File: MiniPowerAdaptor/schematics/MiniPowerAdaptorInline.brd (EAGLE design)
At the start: 20.3 x 19.1 mm, 8 parts, among them IC1 LM317MBSTT3

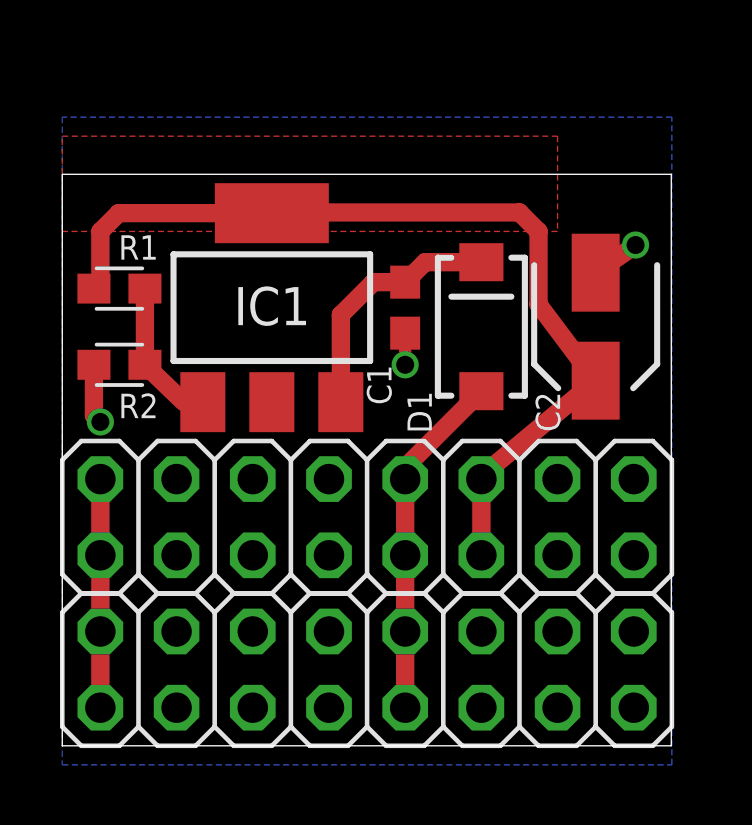
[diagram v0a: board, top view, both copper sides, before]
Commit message: inline 5v adaptor ordered from seeed
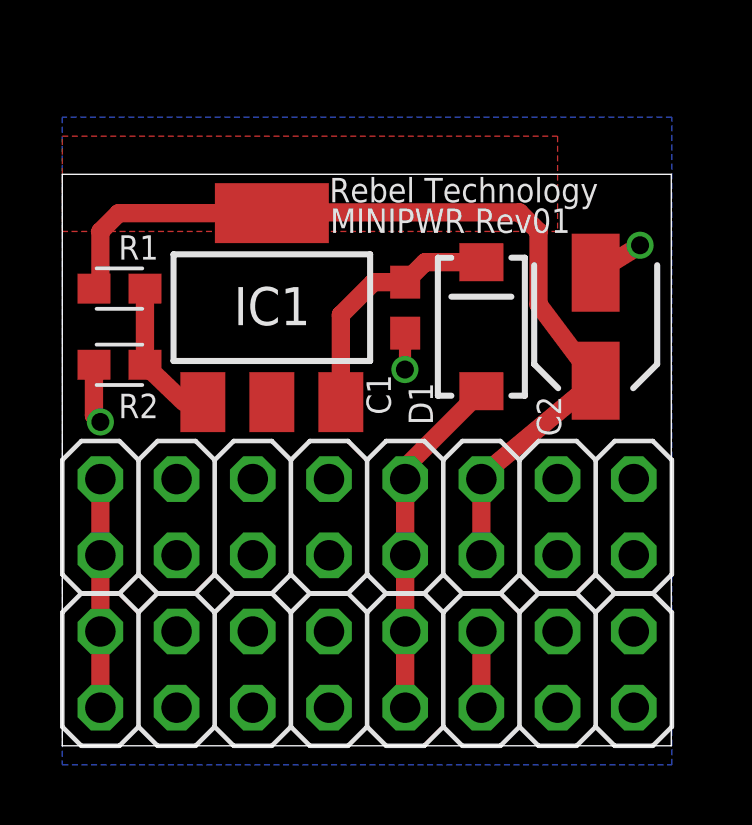
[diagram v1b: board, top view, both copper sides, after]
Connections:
- new net N$2: IN.11, IN.12
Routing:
- net N$2: track 0.00 -> 2.54 mm
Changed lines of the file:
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@@
 <setting verticaltext="up"/>
 </settings>
-<grid distance="0.05" unitdist="inch" unit="inch" style="lines" multiple="1" display="no" altdistance="0.025" altunitdist="inch" altunit="inch"/>
+<grid distance="0.05" unitdist="inch" unit="inch" style="lines" multiple="1" display="no" altdistance="0.000000123031" altunitdist="inch" altunit="inch"/>
 <layers>
 <layer number="1" name="Top" color="4" fill="1" visible="yes" active="yes"/>
-<layer number="2" name="Route2" color="1" fill="3" visible="no" active="no"/>
+<layer number="2" name="Route2" color="1" fill="3" visible="no" active="yes"/>
 <layer number="3" name="Route3" color="4" fill="3" visible="no" active="no"/>
 <layer number="14" name="Route14" color="1" fill="6" visible="no" active="no"/>
-<layer number="15" name="Route15" color="4" fill="6" visible="no" active="no"/>
+<layer number="15" name="Route15" color="4" fill="6" visible="no" active="yes"/>
 <layer number="16" name="Bottom" color="1" fill="1" visible="yes" active="yes"/>
 <layer number="17" name="Pads" color="2" fill="1" visible="yes" active="yes"/>
@@
 <wire x1="21.57" y1="20.32" x2="1.27" y2="20.32" width="0" layer="20"/>
 <wire x1="1.27" y1="20.32" x2="1.27" y2="1.27" width="0" layer="20"/>
-<text x="10.199321875" y="18.365740625" size="0.8128" layer="48" font="vector">MINIPWR Rev01</text>
-<text x="10.173109375" y="19.386709375" size="0.8128" layer="48" font="vector">Rebel Technology</text>
+<text x="10.199321875" y="18.365740625" size="0.8128" layer="21" font="vector">MINIPWR Rev01</text>
+<text x="10.173109375" y="19.386709375" size="0.8128" layer="21" font="vector">Rebel Technology</text>
 <dimension x1="21.57" y1="1.27" x2="1.27" y2="1.27" x3="11.42" y3="-2.54" textsize="1.778" layer="48"/>
 <dimension x1="1.27" y1="1.27" x2="1.27" y2="20.32" x3="0" y3="10.795" textsize="1.778" layer="48"/>
 <text x="20.333109375" y="18.751709375" size="1.27" layer="22" font="vector" rot="MR0">Rebel Technology</text>
+<text x="20.333109375" y="14.941709375" size="1.27" layer="22" font="vector" rot="MR0">MINIPWR Rev01</text>
 </plain>
 <attributes>
@@
 </class>
 </classes>
-<designrules name="Rebel *">
+<designrules name="Rebel">
 <description language="de">
 &lt;b&gt;Rebel Rules&lt;/b&gt;
@@
 &lt;p&gt;
 </description>
-<param name="layerSetup" value="(1*16)"/>
+<param name="layerSetup" value="(1*2+15*16)"/>
 <param name="mtCopper" value="0.035mm 0.035mm 0.035mm 0.035mm 0.035mm 0.035mm 0.035mm 0.035mm 0.035mm 0.035mm 0.035mm 0.035mm 0.035mm 0.035mm 0.035mm 0.035mm"/>
 <param name="mtIsolate" value="1.5mm 0.15mm 0.2mm 0.15mm 0.2mm 0.15mm 0.2mm 0.15mm 0.2mm 0.15mm 0.2mm 0.15mm 0.2mm 0.15mm 0.2mm"/>
@@
 </element>
 <element name="C1" library="rcl" package="C0603" value="100n" x="12.7" y="15.875" smashed="yes" rot="R90">
-<attribute name="NAME" x="11.43" y="13.97" size="0.8128" layer="25" rot="R270"/>
+<attribute name="NAME" x="11.4114" y="13.64455625" size="0.8128" layer="25" rot="R270"/>
 </element>
 <element name="OUT" library="SparkFun" package="2X8" value="M08X2" x="2.54" y="7.62" smashed="yes"/>
 <element name="C2" library="rcl" package="SANYO-OSCON_SMD_A5" value="1u" x="19.05" y="15.24" smashed="yes" rot="R270">
-<attribute name="NAME" x="17.867659375" y="11.731425" size="0.8128" layer="25" rot="R90"/>
+<attribute name="NAME" x="17.899821875" y="11.586775" size="0.8128" layer="25" rot="R90"/>
 </element>
 <element name="D1" library="SparkFun" package="SMA-DIODE" value="" x="15.24" y="15.24" smashed="yes" rot="R90">
-<attribute name="NAME" x="13.589" y="11.684" size="0.8128" layer="25" rot="R90"/>
+<attribute name="NAME" x="13.626196875" y="11.9656625" size="0.8128" layer="25" rot="R90"/>
 <attribute name="VALUE" x="13.589" y="15.494" size="0.4064" layer="27" rot="R90"/>
 </element>
@@
 <vertex x="21.59" y="22.225"/>
 </polygon>
-<wire x1="19.05" y1="17.04" x2="20.3797" y2="17.962125" width="0.6096" layer="1"/>
-<via x="20.3797" y="17.962125" extent="1-16" drill="0.6"/>
+<wire x1="19.05" y1="17.04" x2="20.529090625" y2="17.95465625" width="0.6096" layer="1"/>
+<via x="20.529090625" y="17.95465625" extent="1-16" drill="0.6"/>
 <wire x1="2.325" y1="13.97" x2="2.325" y2="12.28" width="0.6096" layer="1"/>
 <wire x1="2.325" y1="12.28" x2="2.54" y2="12.065" width="0.6096" layer="1"/>
 <via x="2.54" y="12.065" extent="1-16" drill="0.6"/>
-<wire x1="12.7" y1="15.025" x2="12.7" y2="13.97" width="0.4064" layer="1"/>
-<via x="12.7" y="13.97" extent="1-16" drill="0.6"/>
+<wire x1="12.7" y1="15.025" x2="12.6907" y2="13.811928125" width="0.4064" layer="1"/>
+<via x="12.6907" y="13.811928125" extent="1-16" drill="0.6"/>
 </signal>
 <signal name="-12V">
@@
 <wire x1="13.365" y1="17.39" x2="12.7" y2="16.725" width="0.6096" layer="1"/>
 </signal>
+<signal name="N$2">
+<contactref element="IN" pad="12"/>
+<contactref element="IN" pad="11"/>
+<wire x1="15.24" y1="2.54" x2="15.24" y2="5.08" width="0.6096" layer="1"/>
+</signal>
 </signals>

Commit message: changed to dpak, changed electrolytic to 1206 cap and re-routed
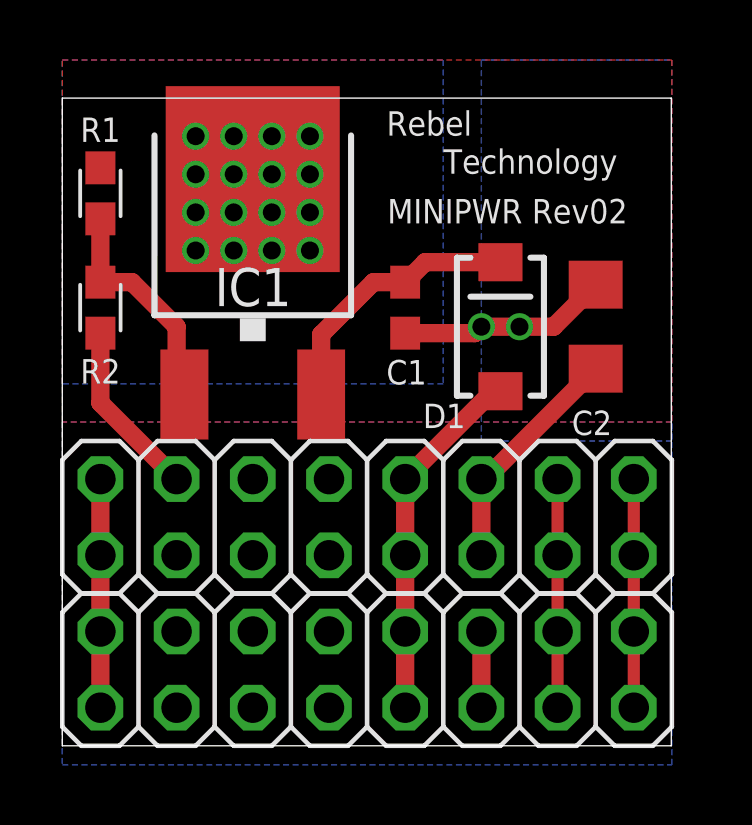
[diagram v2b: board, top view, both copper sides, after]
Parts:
- C2: value 1u -> 10u; device rcl:SANYO-OSCON_SMD_A5 -> rcl:C1206
- D1: value (none) -> S1J
- IC1: value LM317MBSTT3 -> LM317; device v-reg:SOT223 -> v-reg:DPACK
- R1: value 240R -> 330R
- R2: value 720R -> 1k
- moved R1 3.24 mm to (2.54, 19.7), turned to 90 degrees
- moved IC1 2.01 mm to (7.62, 17.8)
- moved R2 2.01 mm to (2.54, 15.9), turned to 90 degrees
- moved D1 0.63 mm to (15.9, 15.2)
- turned C2 to 90 degrees
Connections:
- new net N$4: IN.13, IN.14, OUT.13, OUT.14
- new net N$5: IN.15, IN.16, OUT.15, OUT.16
- net +5V: now also C2.1; no longer C2.+
- net GND: now also C2.2; no longer C2.-
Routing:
- net +5V: track 30.9 -> 9.49 mm, vias 0 -> 16
- net GND: track 4.95 -> 12.9 mm, vias 3 -> 2
- net N$5: track 0.00 -> 7.62 mm
- net N$4: track 0.00 -> 7.62 mm
- net N$1: track 4.97 -> 7.89 mm
- net N$3: track 8.32 -> 8.97 mm
- added copper zone on layer 16, net +5V
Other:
- board size 20.3 x 19.1 mm -> 20.3 x 21.6 mm
- board text added: "-12v"
- board text added: "MINIPWR Rev02"
- board text added: "Rebel"
- board text added: "Technology"
- board text removed: "MINIPWR Rev01"
- board text removed: "Rebel Technology"
